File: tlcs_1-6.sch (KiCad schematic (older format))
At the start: 114 parts, among them U3 TLC5941, U4 TLC5941, U5 TLC5941, U6 TLC5941, U7 TLC5941, U8 TLC5941

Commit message: change to 4-layer, footprint changes, added thermal planes
changed to 4-layer PCB, use internal layer3 for VIN thermal dissipation, bottom layer for GND driver IC dissipation
changed chip CMD resistors & capacitors to use updated library footprints
changed C5 from 0805 to 1206 size (better for 10uF) - needs new BOM part choosing
set up bottom GND copper shape to fill whole board, and added thermal relief (will need to remove for driver IC pads)
added top VIN copper for LEDs (no thermal relief) and vias to connect to layer3 plane
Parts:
- C10, C11, C6, C7, C8, C9: footprint SM0805 -> Capacitors_SMD:C_0805
- R3, R4, R5, R6, R7, R8: footprint SM0805 -> Resistors_SMD:R_0805
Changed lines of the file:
@@
 F 0 "R5" V 4280 5700 40  0000 C CNN
 F 1 "2.2K" V 4207 5701 40  0000 C CNN
-F 2 "SM0805" V 4130 5700 30  0001 C CNN
+F 2 "Resistors_SMD:R_0805" V 4130 5700 30  0001 C CNN
 F 3 "~" H 4200 5700 30  0000 C CNN
 	1    4200 5700
@@
 F 0 "C8" H 4050 5500 40  0000 L CNN
 F 1 "0.1 uF" H 4056 5315 40  0000 L CNN
-F 2 "SM0805" H 4088 5250 30  0001 C CNN
+F 2 "Capacitors_SMD:C_0805" H 4088 5250 30  0001 C CNN
 F 3 "~" H 4050 5400 60  0000 C CNN
 	1    4050 5400
@@
 F 0 "R4" V 4280 3350 40  0000 C CNN
 F 1 "2.2K" V 4207 3351 40  0000 C CNN
-F 2 "SM0805" V 4130 3350 30  0001 C CNN
+F 2 "Resistors_SMD:R_0805" V 4130 3350 30  0001 C CNN
 F 3 "~" H 4200 3350 30  0000 C CNN
 	1    4200 3350
@@
 F 0 "C7" H 4050 3150 40  0000 L CNN
 F 1 "0.1 uF" H 4056 2965 40  0000 L CNN
-F 2 "SM0805" H 4088 2900 30  0001 C CNN
+F 2 "Capacitors_SMD:C_0805" H 4088 2900 30  0001 C CNN
 F 3 "~" H 4050 3050 60  0000 C CNN
 	1    4050 3050
@@
 F 0 "R3" V 4100 1100 40  0000 C CNN
 F 1 "2.2K" V 4300 1100 40  0000 C CNN
-F 2 "SM0805" V 4130 1100 30  0001 C CNN
+F 2 "Resistors_SMD:R_0805" V 4130 1100 30  0001 C CNN
 F 3 "~" H 4200 1100 30  0000 C CNN
 	1    4200 1100
@@
 F 0 "C6" H 4050 900 40  0000 L CNN
 F 1 "0.1 uF" H 4056 715 40  0000 L CNN
-F 2 "SM0805" H 4088 650 30  0001 C CNN
+F 2 "Capacitors_SMD:C_0805" H 4088 650 30  0001 C CNN
 F 3 "~" H 4050 800 60  0000 C CNN
 	1    4050 800
@@
 F 0 "R8" V 9830 5050 40  0000 C CNN
 F 1 "2.2K" V 9757 5051 40  0000 C CNN
-F 2 "SM0805" V 9680 5050 30  0001 C CNN
+F 2 "Resistors_SMD:R_0805" V 9680 5050 30  0001 C CNN
 F 3 "~" H 9750 5050 30  0000 C CNN
 	1    9750 5050
@@
 F 0 "C11" H 9600 4850 40  0000 L CNN
 F 1 "0.1 uF" H 9606 4665 40  0000 L CNN
-F 2 "SM0805" H 9638 4600 30  0001 C CNN
+F 2 "Capacitors_SMD:C_0805" H 9638 4600 30  0001 C CNN
 F 3 "~" H 9600 4750 60  0000 C CNN
 	1    9600 4750
@@
 F 0 "R6" V 9830 1050 40  0000 C CNN
 F 1 "2.2K" V 9757 1051 40  0000 C CNN
-F 2 "SM0805" V 9680 1050 30  0001 C CNN
+F 2 "Resistors_SMD:R_0805" V 9680 1050 30  0001 C CNN
 F 3 "~" H 9750 1050 30  0000 C CNN
 	1    9750 1050
@@
 F 0 "C9" H 9600 850 40  0000 L CNN
 F 1 "0.1 uF" H 9606 665 40  0000 L CNN
-F 2 "SM0805" H 9638 600 30  0001 C CNN
+F 2 "Capacitors_SMD:C_0805" H 9638 600 30  0001 C CNN
 F 3 "~" H 9600 750 60  0000 C CNN
 	1    9600 750
@@
 F 0 "C10" H 9600 2850 40  0000 L CNN
 F 1 "0.1 uF" H 9606 2665 40  0000 L CNN
-F 2 "SM0805" H 9638 2600 30  0001 C CNN
+F 2 "Capacitors_SMD:C_0805" H 9638 2600 30  0001 C CNN
 F 3 "~" H 9600 2750 60  0000 C CNN
 	1    9600 2750
@@
 F 0 "R7" V 9830 3050 40  0000 C CNN
 F 1 "2.2K" V 9757 3051 40  0000 C CNN
-F 2 "SM0805" V 9680 3050 30  0001 C CNN
+F 2 "Resistors_SMD:R_0805" V 9680 3050 30  0001 C CNN
 F 3 "~" H 9750 3050 30  0000 C CNN
 	1    9750 3050

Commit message: symbol & footprint library changes, plus LED driver signal routing
done some more routing of central LED driver signals on IN1 layer
created new 'lpa96_symbols.lib' schematic library and moved existing symbols from tca-rescue to there (except commodity ones, will take from main KiCAD library)
changed footprint for TLC5941 (downloaded from TI official, via ultralibrarian, generated for IPC 'most'), still needs some tweaks
added pin29 for thermal pad to TLC5941 symbol (to match new footprint), needs connecting in schematic still
deleted obsolete .mod footprint files, and also double_led, myParts, Resonator_3pins and Cer_reso symbol libraries (old parts no longer used, or now in new lpa96_symbols library)
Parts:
- U3, U4, U5, U6, U7, U8: footprint TLC5940_FIXED -> tca_footprints:TLC5941_PWP_28; symbol tca-rescue:TLC5941 -> lpa96_symbols:TLC5941
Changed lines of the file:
@@
 	4050 600  4450 600
 $Comp
-L tca-rescue:TLC5941 U5
+L lpa96_symbols:TLC5941 U5
 U 1 1 53AA07FE
 P 3000 6250
 F 0 "U5" H 3000 6150 50  0000 C CNN
 F 1 "TLC5941" H 3000 6350 50  0000 C CNN
-F 2 "TLC5940_FIXED" H 3000 6250 50  0001 C CNN
+F 2 "tca_footprints:TLC5941_PWP_28" H 3000 6250 50  0001 C CNN
 F 3 "DOCUMENTATION" H 3000 6250 50  0001 C CNN
 	1    3000 6250
@@
 $EndComp
 $Comp
-L tca-rescue:TLC5941 U4
+L lpa96_symbols:TLC5941 U4
 U 1 1 536301A0
 P 3000 3900
 F 0 "U4" H 3000 3800 50  0000 C CNN
 F 1 "TLC5941" H 3000 4000 50  0000 C CNN
-F 2 "TLC5940_FIXED" H 3000 3900 50  0001 C CNN
+F 2 "tca_footprints:TLC5941_PWP_28" H 3000 3900 50  0001 C CNN
 F 3 "DOCUMENTATION" H 3000 3900 50  0001 C CNN
 	1    3000 3900
@@
 $EndComp
 $Comp
-L tca-rescue:TLC5941 U3
+L lpa96_symbols:TLC5941 U3
 U 1 1 53630973
 P 3000 1650
 F 0 "U3" H 3000 1550 50  0000 C CNN
 F 1 "TLC5941" H 3000 1750 50  0000 C CNN
-F 2 "TLC5940_FIXED" H 3000 1650 50  0001 C CNN
+F 2 "tca_footprints:TLC5941_PWP_28" H 3000 1650 50  0001 C CNN
 F 3 "DOCUMENTATION" H 3000 1650 50  0001 C CNN
 	1    3000 1650
@@
 	9600 550  10000 550
 $Comp
-L tca-rescue:TLC5941 U8
+L lpa96_symbols:TLC5941 U8
 U 1 1 53630E91
 P 8550 5600
 F 0 "U8" H 8550 5500 50  0000 C CNN
 F 1 "TLC5941" H 8550 5700 50  0000 C CNN
-F 2 "TLC5940_FIXED" H 8550 5600 50  0001 C CNN
+F 2 "tca_footprints:TLC5941_PWP_28" H 8550 5600 50  0001 C CNN
 F 3 "DOCUMENTATION" H 8550 5600 50  0001 C CNN
 	1    8550 5600
@@
 $EndComp
 $Comp
-L tca-rescue:TLC5941 U6
+L lpa96_symbols:TLC5941 U6
 U 1 1 53630EE8
 P 8550 1600
 F 0 "U6" H 8550 1500 50  0000 C CNN
 F 1 "TLC5941" H 8550 1700 50  0000 C CNN
-F 2 "TLC5940_FIXED" H 8550 1600 50  0001 C CNN
+F 2 "tca_footprints:TLC5941_PWP_28" H 8550 1600 50  0001 C CNN
 F 3 "DOCUMENTATION" H 8550 1600 50  0001 C CNN
 	1    8550 1600
@@
 NoConn ~ 9300 3450
 $Comp
-L tca-rescue:TLC5941 U7
+L lpa96_symbols:TLC5941 U7
 U 1 1 53630EB0
 P 8550 3600
 F 0 "U7" H 8550 3500 50  0000 C CNN
 F 1 "TLC5941" H 8550 3700 50  0000 C CNN
-F 2 "TLC5940_FIXED" H 8550 3600 50  0001 C CNN
+F 2 "tca_footprints:TLC5941_PWP_28" H 8550 3600 50  0001 C CNN
 F 3 "DOCUMENTATION" H 8550 3600 50  0001 C CNN
 	1    8550 3600

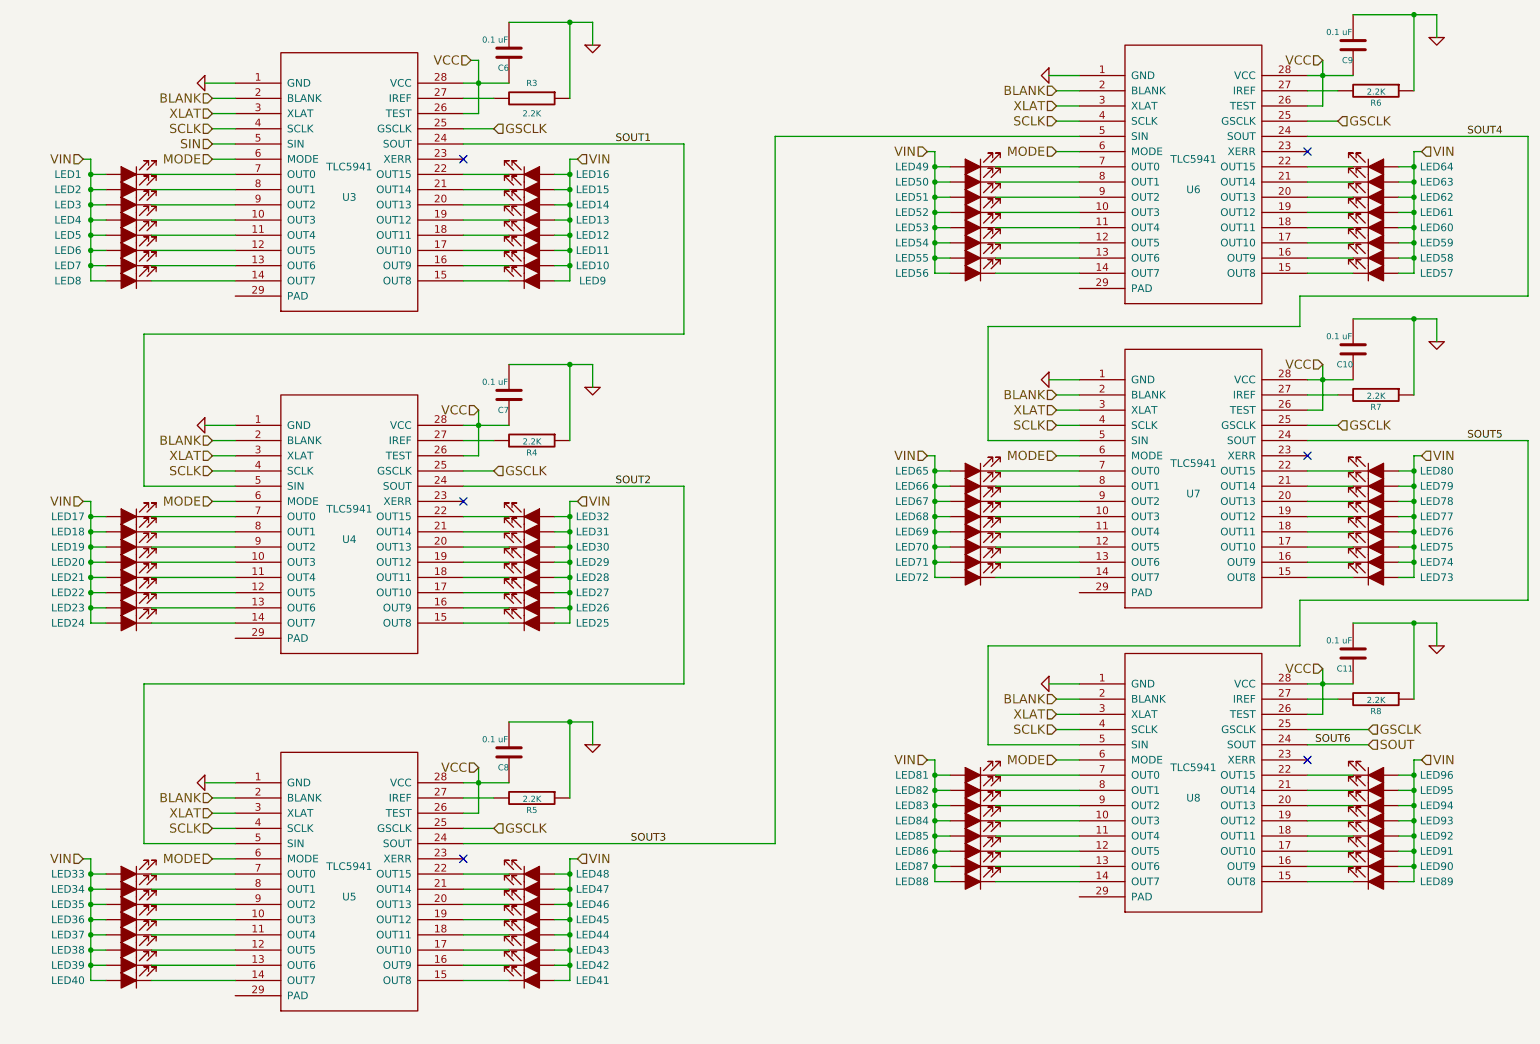
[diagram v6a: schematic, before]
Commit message: power supply improvements & routing, footprint and other tweaks
added extra bulk cap C12 for VCC on LED driver page, placed near LED drivers
connected pin29 of new TLC5941 symbol to GND and changed pad to be solid connection to plane
finished placement of decoupling caps near drivers, and VCC routing/plane/vias for drivers
small thermal via tweaks
changed keepout near SDCARD to apply to copper planes too
finished the routing around input and regulator
deleted POWER net class, gets in the way of VCC fanout routing and nothing really needs separate design rules (shape separation controlled in shape or manually)
added 3D model to TLC5941 library part, tweaked silkscreen to improve polarity dot & put REF outside part, refreshed in PCB design
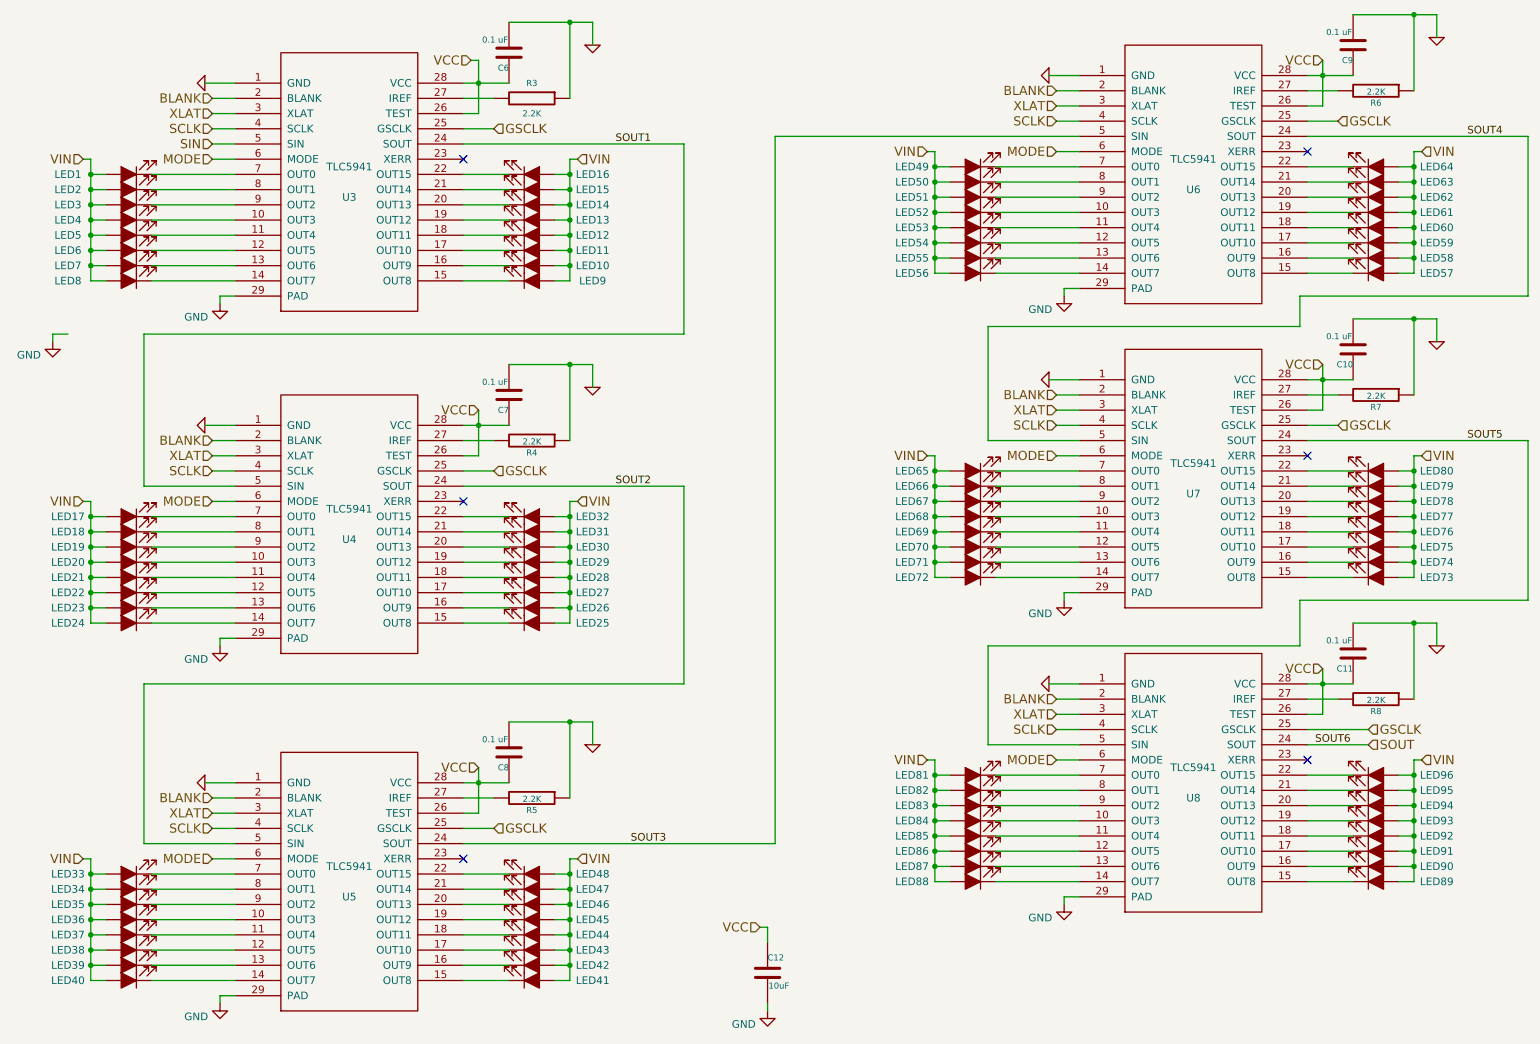
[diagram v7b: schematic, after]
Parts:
- added C12: 10uF, Capacitors_SMD:C_1206, symbol tca-rescue:C
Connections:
- net GND: now also U3.29 (PAD), U4.29 (PAD), U5.29 (PAD), U6.29 (PAD), U7.29 (PAD), U8.29 (PAD), C12.2
- net VCC: now also C12.1
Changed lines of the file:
@@
 	5200 2650 5200 1400
-Wire Wire Line
-	1650 2650 5200 2650
 Wire Wire Line
 	5200 1400 3750 1400
@@
 Wire Wire Line
 	9300 5350 9700 5350
+$Comp
+L power:GND #PWR0101
+U 1 1 5D60C7F0
+P 2150 2450
+F 0 "#PWR0101" H 2150 2200 50  0001 C CNN
+F 1 "GND" H 2072 2333 50  0000 R BNN
+F 2 "" H 2150 2450 50  0001 C CNN
+F 3 "" H 2150 2450 50  0001 C CNN
+	1    2150 2450
+	1    0    0    -1
+$EndComp
+Wire Wire Line
+	2250 2400 2150 2400
+Wire Wire Line
+	2150 2450 2150 2400
+$Comp
+L power:GND #PWR0102
+U 1 1 5D76EF32
+P 1050 2700
+F 0 "#PWR0102" H 1050 2450 50  0001 C CNN
+F 1 "GND" H 972 2583 50  0000 R BNN
+F 2 "" H 1050 2700 50  0001 C CNN
+F 3 "" H 1050 2700 50  0001 C CNN
+	1    1050 2700
+	1    0    0    -1
+$EndComp
+Wire Wire Line
+	1150 2650 1050 2650
+Wire Wire Line
+	1050 2700 1050 2650
+$Comp
+L power:GND #PWR0103
+U 1 1 5D7A2AEB
+P 2150 4700
+F 0 "#PWR0103" H 2150 4450 50  0001 C CNN
+F 1 "GND" H 2072 4583 50  0000 R BNN
+F 2 "" H 2150 4700 50  0001 C CNN
+F 3 "" H 2150 4700 50  0001 C CNN
+	1    2150 4700
+	1    0    0    -1
+$EndComp
+Wire Wire Line
+	2250 4650 2150 4650
+Wire Wire Line
+	2150 4700 2150 4650
+$Comp
+L power:GND #PWR0104
+U 1 1 5D7D8305
+P 2150 7050
+F 0 "#PWR0104" H 2150 6800 50  0001 C CNN
+F 1 "GND" H 2072 6933 50  0000 R BNN
+F 2 "" H 2150 7050 50  0001 C CNN
+F 3 "" H 2150 7050 50  0001 C CNN
+	1    2150 7050
+	1    0    0    -1
+$EndComp
+Wire Wire Line
+	2250 7000 2150 7000
+Wire Wire Line
+	2150 7050 2150 7000
+$Comp
+L power:GND #PWR0105
+U 1 1 5D80D19F
+P 7700 2400
+F 0 "#PWR0105" H 7700 2150 50  0001 C CNN
+F 1 "GND" H 7622 2283 50  0000 R BNN
+F 2 "" H 7700 2400 50  0001 C CNN
+F 3 "" H 7700 2400 50  0001 C CNN
+	1    7700 2400
+	1    0    0    -1
+$EndComp
+Wire Wire Line
+	7800 2350 7700 2350
+Wire Wire Line
+	7700 2400 7700 2350
+$Comp
+L power:GND #PWR0106
+U 1 1 5D842CB1
+P 7700 4400
+F 0 "#PWR0106" H 7700 4150 50  0001 C CNN
+F 1 "GND" H 7622 4283 50  0000 R BNN
+F 2 "" H 7700 4400 50  0001 C CNN
+F 3 "" H 7700 4400 50  0001 C CNN
+	1    7700 4400
+	1    0    0    -1
+$EndComp
+Wire Wire Line
+	7800 4350 7700 4350
+Wire Wire Line
+	7700 4400 7700 4350
+$Comp
+L power:GND #PWR0107
+U 1 1 5D878F26
+P 7700 6400
+F 0 "#PWR0107" H 7700 6150 50  0001 C CNN
+F 1 "GND" H 7622 6283 50  0000 R BNN
+F 2 "" H 7700 6400 50  0001 C CNN
+F 3 "" H 7700 6400 50  0001 C CNN
+	1    7700 6400
+	1    0    0    -1
+$EndComp
+Wire Wire Line
+	7800 6350 7700 6350
+Wire Wire Line
+	7700 6400 7700 6350
+Wire Wire Line
+	1650 2650 5200 2650
+$Comp
+L tca-rescue:C C?
+U 1 1 5D98BF30
+P 5750 6850
+AR Path="/5D98BF30" Ref="C?"  Part="1"
+AR Path="/5362FF20/5D98BF30" Ref="C12"  Part="1"
+F 0 "C12" H 5750 6950 40  0000 L CNN
+F 1 "10uF" H 5756 6765 40  0000 L CNN
+F 2 "Capacitors_SMD:C_1206" H 5788 6700 30  0001 C CNN
+F 3 "~" H 5750 6850 60  0000 C CNN
+	1    5750 6850
+	1    0    0    -1
+$EndComp
+$Comp
+L power:GND #PWR019
+U 1 1 5D9C0F54
+P 5750 7100
+F 0 "#PWR019" H 5750 6850 50  0001 C CNN
+F 1 "GND" H 5672 6983 50  0000 R BNN
+F 2 "" H 5750 7100 50  0001 C CNN
+F 3 "" H 5750 7100 50  0001 C CNN
+	1    5750 7100
+	1    0    0    -1
+$EndComp
+Wire Wire Line
+	5750 7050 5750 7100
+Text HLabel 5700 6550 0    60   Input ~ 0
+VCC
+Wire Wire Line
+	5700 6550 5750 6550
+Wire Wire Line
+	5750 6550 5750 6650
 $EndSCHEMATC

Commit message: renamed refdes for some parts, library changes, adding 3d models
renamed library, both folder and the reference in KiCAD to remove old 'tca' reference, updated other references to match
added 3d models for input caps and reset switch from KiCad main library (locally in design)
changed all resistors and GNDs to use symbols from main KiCAD library
renamed R_ON1,R_ERR1,R_FIN1 as R9,R10,R11 (best practice)
renamed RESET1 as SW1 and ON1,ERR1,FIN1 as LED97,LED98,LED99 (best practice)
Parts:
- LED1, LED10, LED11, LED12, LED13, LED14, LED15, LED16, LED17, LED18, LED19, LED2, LED20, LED21, LED22, LED23, LED24, LED25, LED26, LED27, LED28, LED29, LED3, LED30, LED31, LED32, LED33, LED34, LED35, LED36, LED37, LED38, LED39, LED4, LED40, LED41, LED42, LED43, LED44, LED45, LED46, LED47, LED48, LED49, LED5, LED50, LED51, LED52, LED53, LED54, LED55, LED56, LED57, LED58, LED59, LED6, LED60, LED61, LED62, LED63, LED64, LED65, LED66, LED67, LED68, LED69, LED7, LED70, LED71, LED72, LED73, LED74, LED75, LED76, LED77, LED78, LED79, LED8, LED80, LED81, LED82, LED83, LED84, LED85, LED86, LED87, LED88, LED89, LED9, LED90, LED91, LED92, LED93, LED94, LED95, LED96: footprint tca_footprints:VLDx1232G -> lpa96_footprints:VLDx1232G
- R3, R4, R5, R6, R7, R8: symbol tca-rescue:R -> Device:R
- U3, U4, U5, U6, U7, U8: footprint tca_footprints:TLC5941_PWP_28 -> lpa96_footprints:TLC5941_PWP_28
